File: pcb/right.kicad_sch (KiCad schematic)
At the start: 59 parts, among them J1 Conn_01x15_Pin, J2 USB_C_Receptacle_USB2.0_16P, J3 Conn_01x02_Socket, J4 Conn_01x15_Pin, J5 Conn_ARM_SWD_TagConnect_TC203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, J6 Conn_01x15_Pin, Q1 IRLML6402, SW1 MX_SW_HS, SW10 MX_SW_HS, SW11 MX_SW_HS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

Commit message: added ESD-protection
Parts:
- added C9: 10u, Capacitor_SMD:C_0603_1608Metric_Pad1.08x0.95mm_HandSolder, symbol Device:C
- added D35, D39: PESD5V0C1ULS-Q., Diode_SMD:D_SOD-882D, symbol Device:D
- added D37: PESD5V0S1UL_315, custom-libary:DIO_PESD5V0S1UL_315, symbol custom-libary:PESD5V0S1UL_315
- added FL1: BLM18KG221SN1D, custom-libary:BEADC1608X95N, symbol custom-libary:BLM18KG221SN1D
- added J13: Conn_01x15_Pin, Connector_FFC-FPC:Hirose_FH12-15S-0.5SH_1x15-1MP_P0.50mm_Horizontal, symbol Connector:Conn_01x15_Pin
- added R17, R18: 1k, Resistor_SMD:R_0603_1608Metric_Pad0.98x0.95mm_HandSolder, symbol Device:R
- R2: value R -> 806k
- R3: value R -> 2M
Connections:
- net D+: now also D39.1 (K)
- net D-: now also D35.1 (K)
- net GND: now also C9.2, D35.2 (A), D37.A, D39.2 (A)
- net SWDCLK: now also R17.2; no longer J5.4 (SWCLK)
- net SWDIO: now also R18.1; no longer J5.2 (SWDIO)
- net VBUS: now also D37.K, FL1.1; no longer U1.32 (VBUS)
- net at J1.1 (Pin_1), J4.1 (Pin_1): now also J13.15 (Pin_15)
- net at J1.10 (Pin_10), J4.10 (Pin_10): now also J13.6 (Pin_6)
- net at J1.11 (Pin_11), J4.11 (Pin_11): now also J13.5 (Pin_5)
- net at J1.12 (Pin_12), J4.12 (Pin_12): now also J13.4 (Pin_4)
- net at J1.13 (Pin_13), J4.13 (Pin_13): now also J13.3 (Pin_3)
- net at J1.14 (Pin_14), J4.14 (Pin_14): now also J13.2 (Pin_2)
- net at J1.15 (Pin_15), J4.15 (Pin_15): now also J13.1 (Pin_1)
- net at J1.2 (Pin_2), J4.2 (Pin_2): now also J13.14 (Pin_14)
- net at J1.3 (Pin_3), J4.3 (Pin_3): now also J13.13 (Pin_13)
- net at J1.4 (Pin_4), J4.4 (Pin_4): now also J13.12 (Pin_12)
- net at J1.5 (Pin_5), J4.5 (Pin_5): now also J13.11 (Pin_11)
- net at J1.6 (Pin_6), J4.6 (Pin_6): now also J13.10 (Pin_10)
- net at J1.7 (Pin_7), J4.7 (Pin_7): now also J13.9 (Pin_9)
- net at J1.8 (Pin_8), J4.8 (Pin_8): now also J13.8 (Pin_8)
- net at J1.9 (Pin_9), J4.9 (Pin_9): now also J13.7 (Pin_7)
- new net: J5.2 (SWDIO), R18.2
- new net: J5.4 (SWCLK), R17.1
- new net VBUS_FIL: C9.1, FL1.2, U1.32 (VBUS)
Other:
- moved on the sheet: C1, C2, C3, C4, D1, D10, D11, D12, D13, D14, D15, D16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

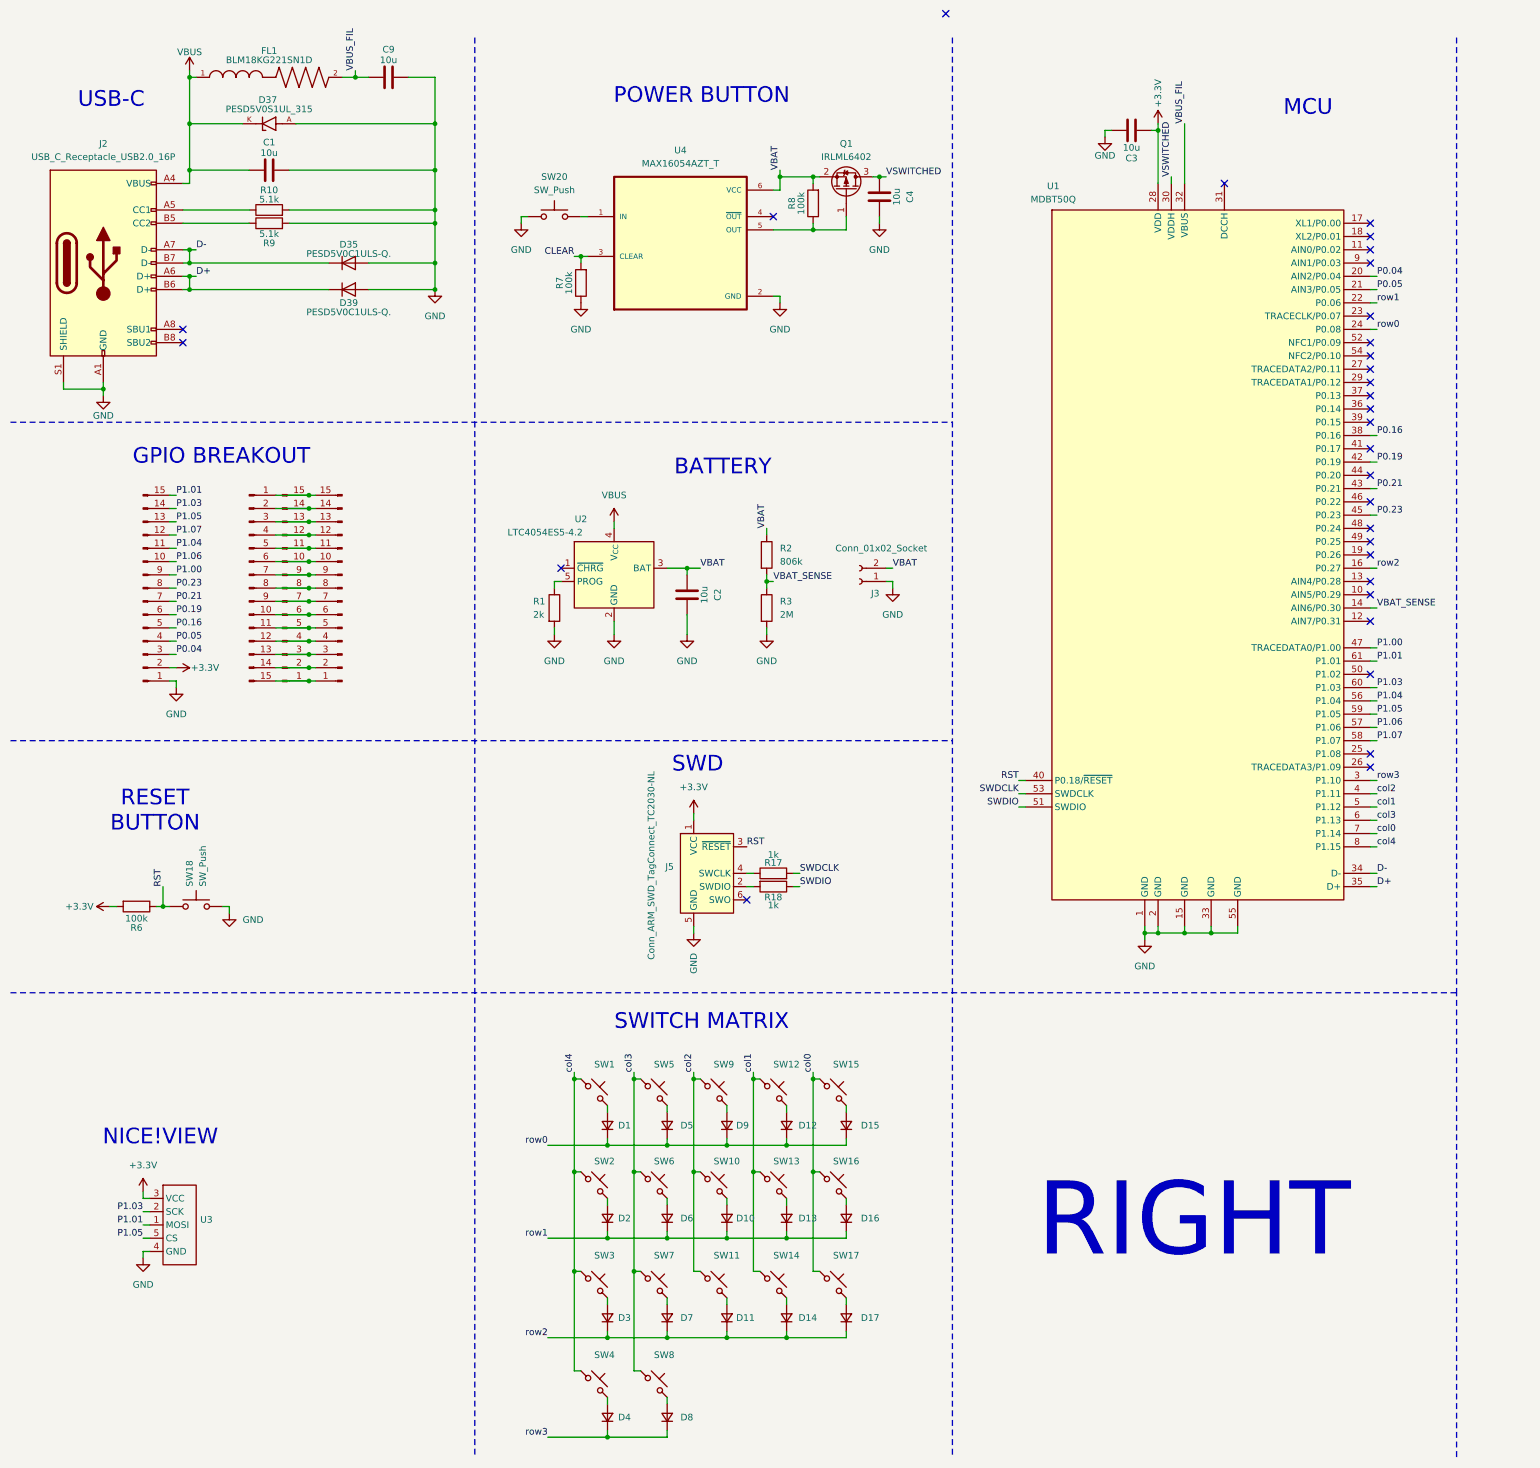
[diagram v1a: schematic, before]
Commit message: added external oszilator
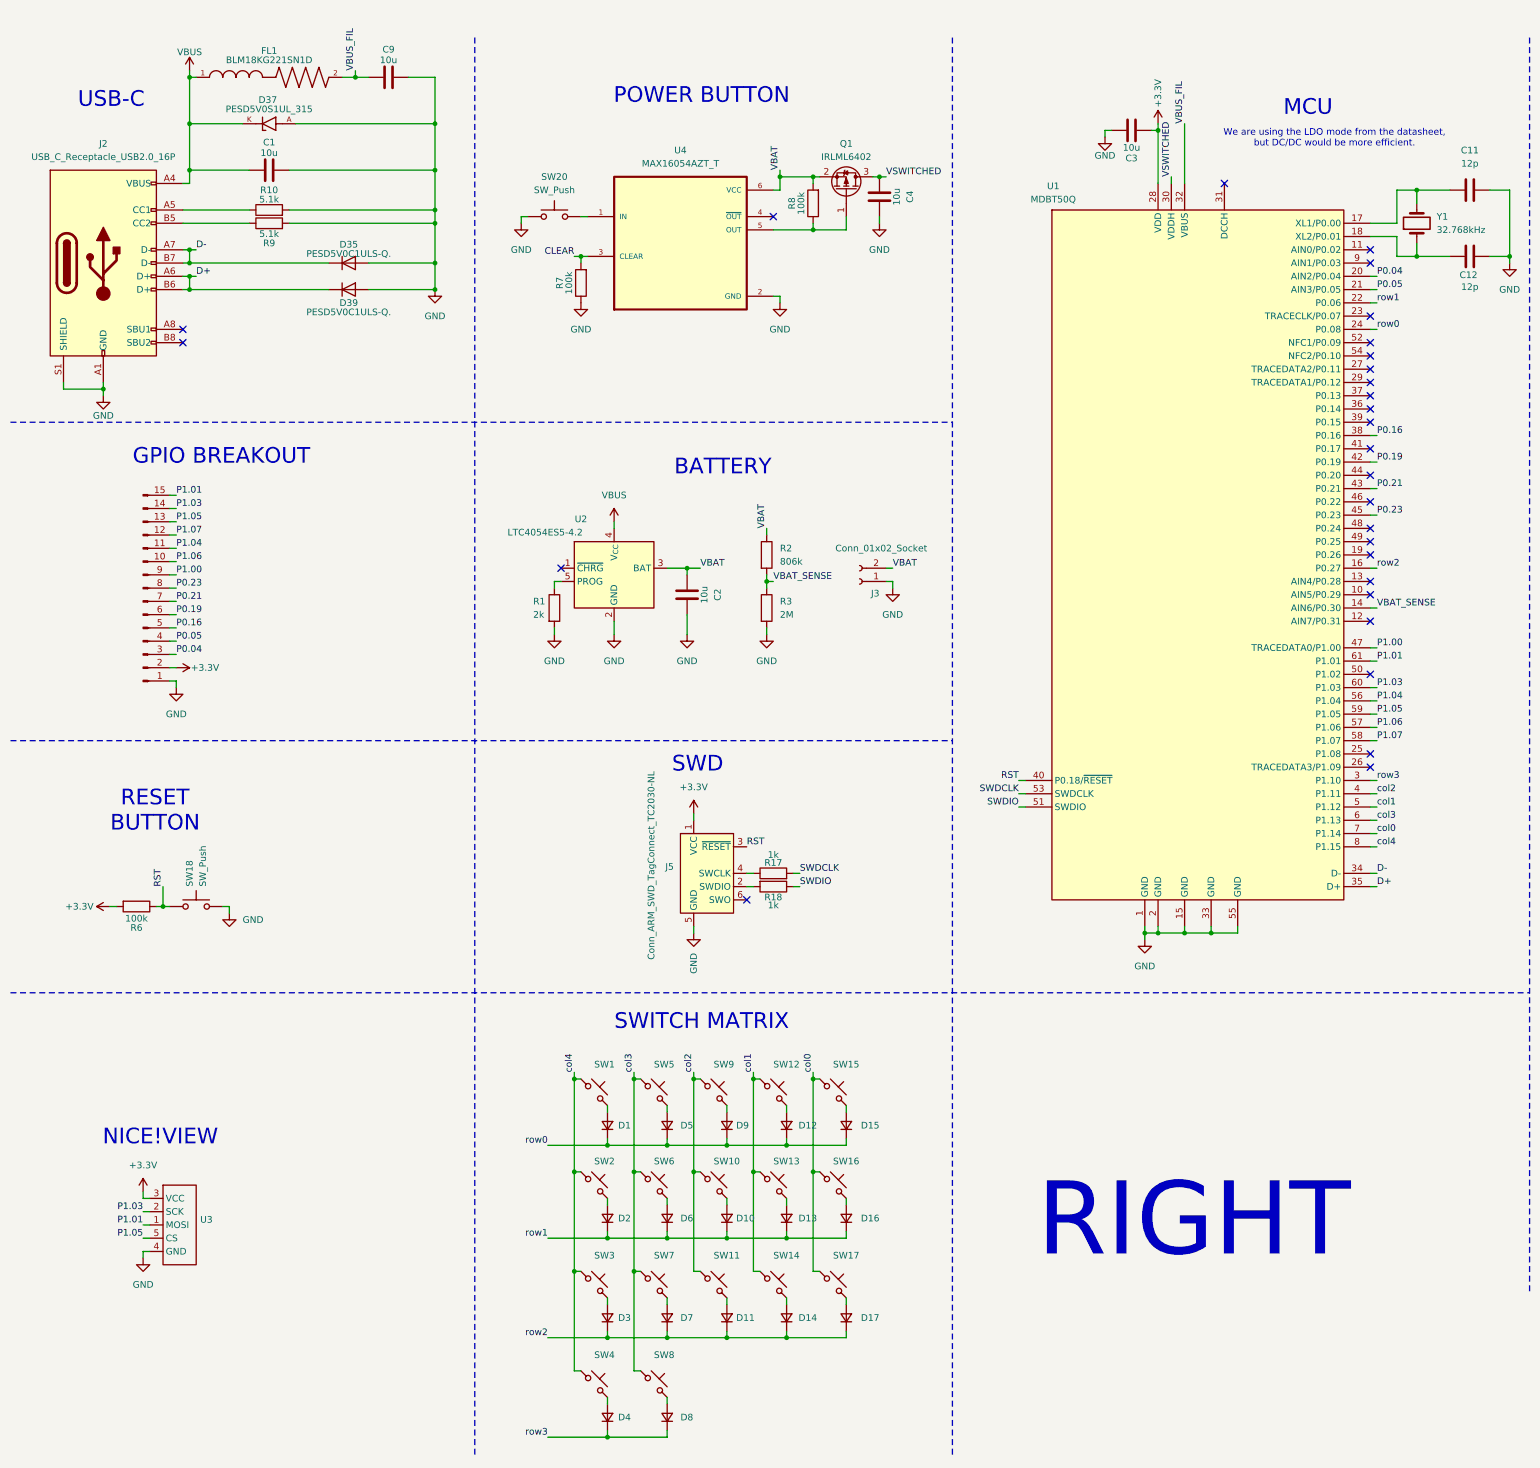
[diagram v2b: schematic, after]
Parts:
- removed J1, J13: Conn_01x15_Pin, Connector_FFC-FPC:Hirose_FH12-15S-0.5SH_1x15-1MP_P0.50mm_Horizontal, symbol Connector:Conn_01x15_Pin
- removed J4: Conn_01x15_Pin, Connector_PinHeader_2.54mm:PinHeader_1x15_P2.54mm_Vertical, symbol Connector:Conn_01x15_Pin
- added C11, C12: 12p, Capacitor_SMD:C_0603_1608Metric_Pad1.08x0.95mm_HandSolder, symbol Device:C
- added Y1: 32.768kHz, custom-libary:FC2012SN32768K90NNA0KC0, symbol Device:Crystal
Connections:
- net GND: now also C11.1, C12.1
- net at U1.17 (XL1/P0.00): now also C11.2, Y1.2
- net at U1.18 (XL2/P0.01): now also C12.2, Y1.1
- no-connect marks 31 -> 28
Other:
- note added: "We are using the LDO mode from the datasheet, but DC/DC would be more efficient."

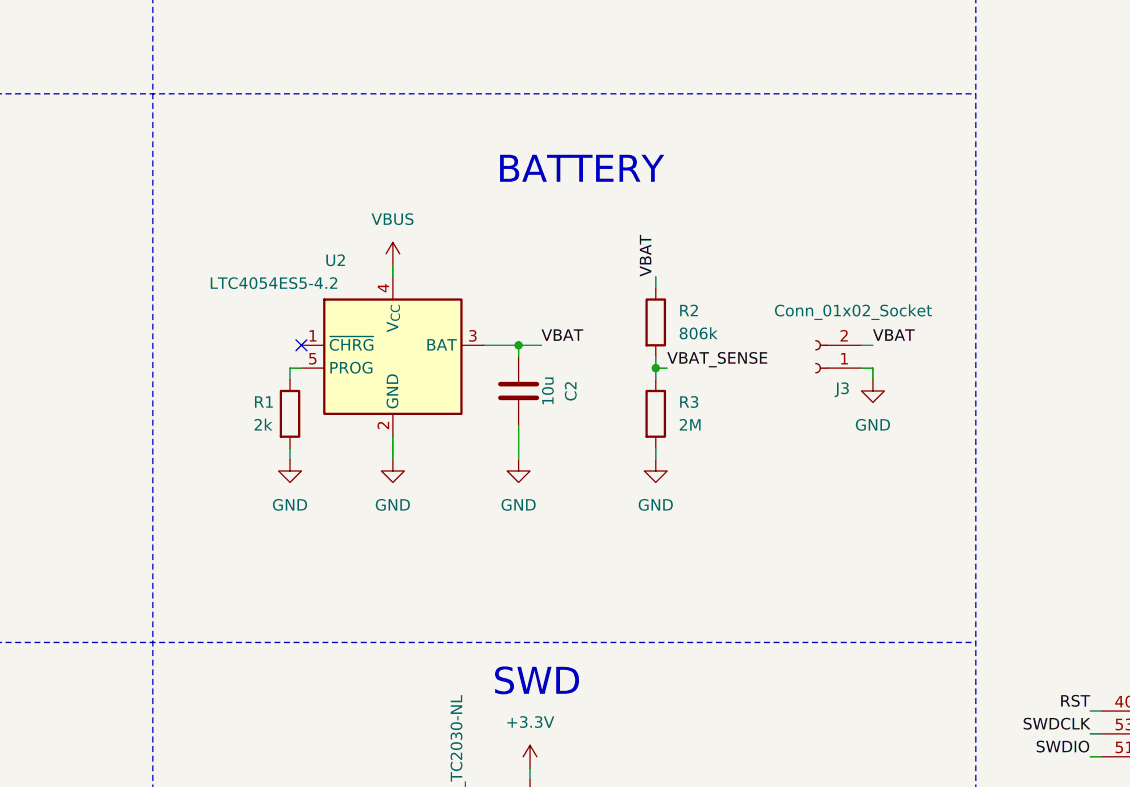
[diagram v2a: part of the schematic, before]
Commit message: replaced charge circuit for cost reasons
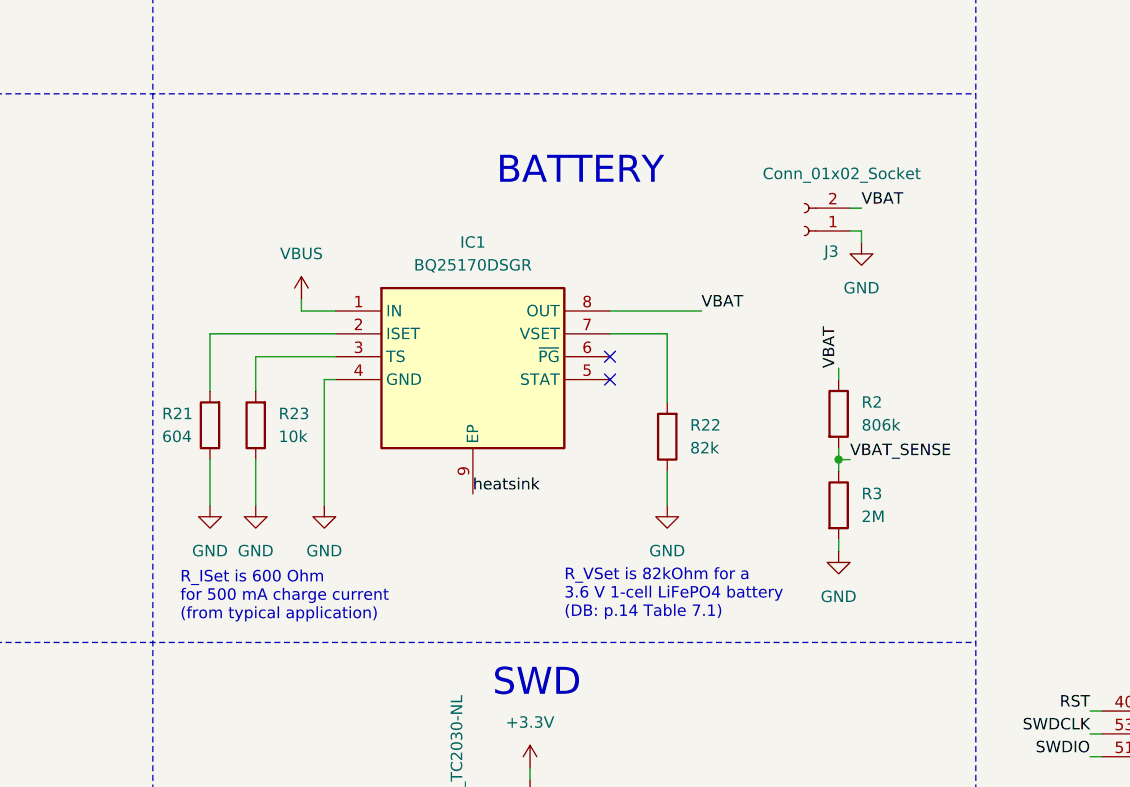
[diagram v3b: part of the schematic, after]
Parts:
- removed C2: 10u, Capacitor_SMD:C_0603_1608Metric_Pad1.08x0.95mm_HandSolder, symbol Device:C
- removed R1: 2k, Resistor_SMD:R_0603_1608Metric_Pad0.98x0.95mm_HandSolder, symbol Device:R
- removed U2: LTC4054ES5-4.2, Package_TO_SOT_SMD:TSOT-23-5, symbol Battery_Management:LTC4054ES5-4.2
- added IC1: BQ25170DSGR, SON50P200X200X80-9N, symbol BQ25170DSGR:BQ25170DSGR
- added R21: 604, Resistor_SMD:R_0603_1608Metric_Pad0.98x0.95mm_HandSolder, symbol Device:R
- added R22: 82k, Resistor_SMD:R_0603_1608Metric_Pad0.98x0.95mm_HandSolder, symbol Device:R
- added R23: 10k, Resistor_SMD:R_0603_1608Metric_Pad0.98x0.95mm_HandSolder, symbol Device:R
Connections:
- net GND: now also IC1.4 (GND), R21.1, R22.1, R23.1
- net VBAT: now also IC1.8 (OUT)
- net VBUS: now also IC1.1 (IN)
- new net: IC1.3 (TS), R23.2
- new net: IC1.7 (VSET), R22.2
- new net: IC1.2 (ISET), R21.2
- new net heatsink: IC1.9 (EP)
- no-connect marks 28 -> 29
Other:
- note added: "R_ISet is 600 Ohm for 500 mA charge current (from typical application)"
- note added: "R_VSet is 82kOhm for a 3.6 V 1-cell LiFePO4 battery (DB: p.14 Table 7.1)"
- moved on the sheet: J3, R2, R3

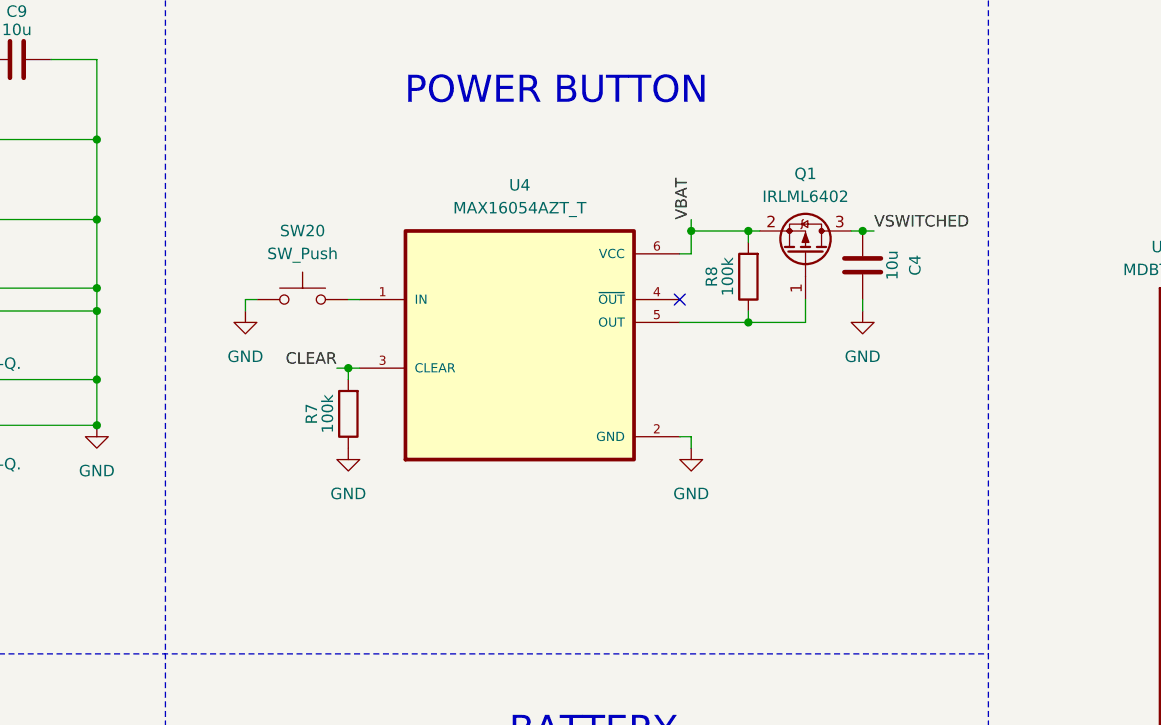
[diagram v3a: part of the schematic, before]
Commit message: replaced button ic and updated bom
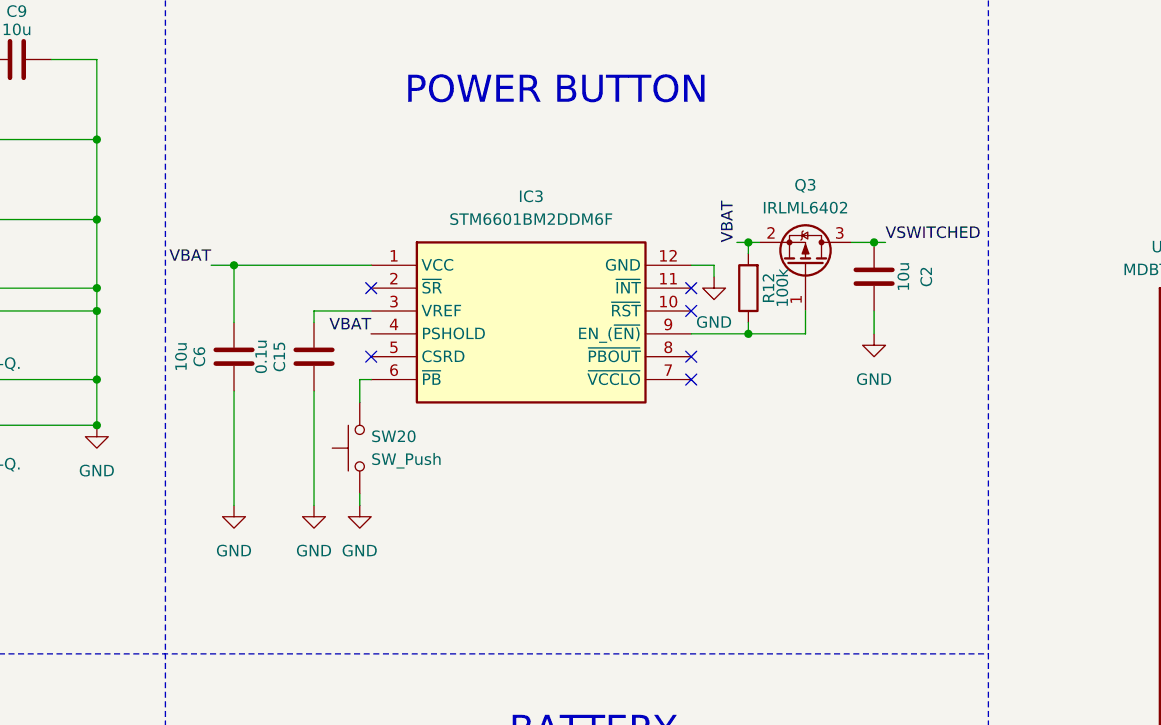
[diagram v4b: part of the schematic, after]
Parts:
- removed C4: 10u, Capacitor_SMD:C_0603_1608Metric_Pad1.08x0.95mm_HandSolder, symbol Device:C
- removed Q1: IRLML6402, Package_TO_SOT_SMD:SOT-23, symbol Transistor_FET:IRLML6402
- removed R7, R8: 100k, Resistor_SMD:R_0603_1608Metric_Pad0.98x0.95mm_HandSolder, symbol Device:R
- removed U4: MAX16054AZT_T, custom-libary:SOT95P275X110-6N, symbol custom-libary:MAX16054AZT_T
- added C15: 0.1u, Capacitor_SMD:C_0603_1608Metric_Pad1.08x0.95mm_HandSolder, symbol Device:C
- added C2, C6: 10u, Capacitor_SMD:C_0603_1608Metric_Pad1.08x0.95mm_HandSolder, symbol Device:C
- added IC3: STM6601BM2DDM6F, custom-libary:STM6601BM2DDM6F, symbol custom-libary:STM6601BM2DDM6F
- added Q3: IRLML6402, Package_TO_SOT_SMD:SOT-23, symbol Transistor_FET:IRLML6402
- added R12: 100k, Resistor_SMD:R_0603_1608Metric_Pad0.98x0.95mm_HandSolder, symbol Device:R
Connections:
- net GND: now also C15.2, C2.2, C6.2, IC3.12 (GND)
- net VBAT: now also C6.1, IC3.1 (VCC), IC3.4 (PSHOLD), Q3.2 (S), R12.2
- net VSWITCHED: now also C2.1, Q3.3 (D)
- net at SW20.2: now also IC3.6 (~{PB})
- new net: IC3.9 (EN_(~{EN)}), Q3.1 (G), R12.1
- new net: C15.1, IC3.3 (VREF)
- no-connect marks 29 -> 34
